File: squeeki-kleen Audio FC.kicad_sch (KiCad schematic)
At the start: 18 parts, among them J1 GND, J2 VCC, J3 P1, J4 P2, J5 C8, J6 GND out, U1 OPA1671IDCKT

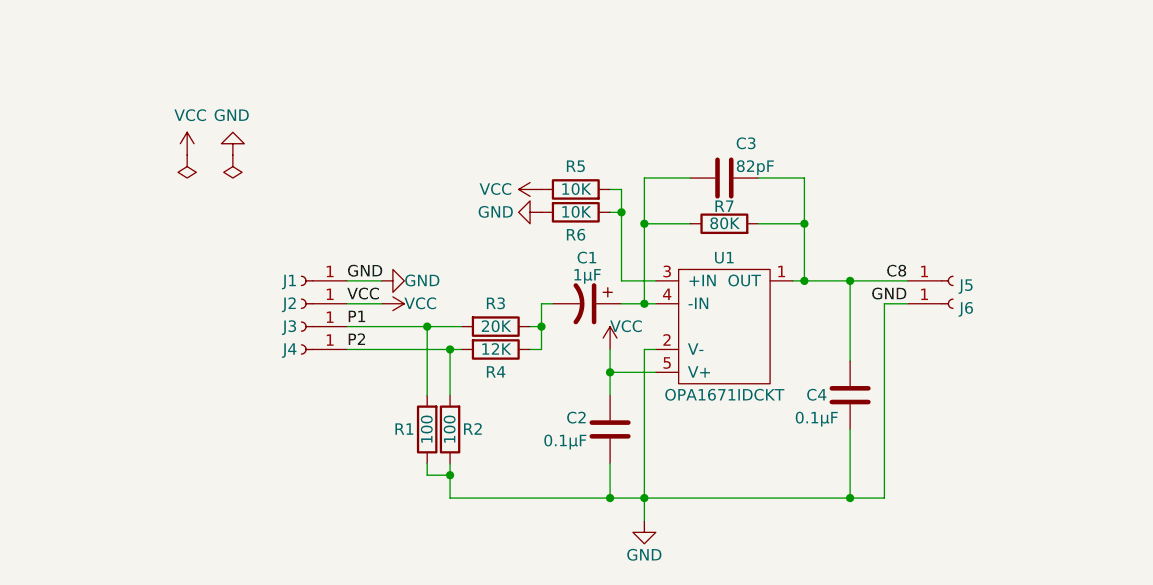
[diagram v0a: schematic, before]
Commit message: Update board layout, add level adjustment
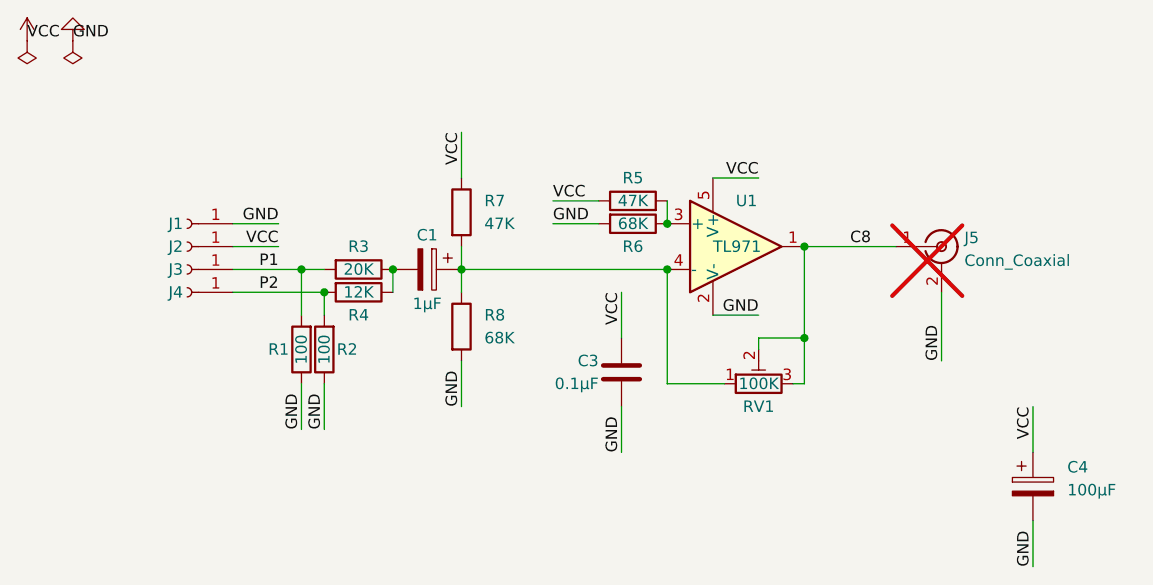
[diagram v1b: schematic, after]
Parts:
- removed C1: 1µF, Capacitor_Tantalum_SMD:CP_EIA-3216-18_Kemet-A_Pad1.58x1.35mm_HandSolder, symbol Device:CP1
- removed C3: 82pF, Capacitor_SMD:C_0805_2012Metric_Pad1.18x1.45mm_HandSolder, symbol Device:C
- removed C4: 0.1µF, Capacitor_SMD:C_0805_2012Metric_Pad1.18x1.45mm_HandSolder, symbol Device:C
- removed J5: C8, custom footprints:Custom_Pad, symbol Connector:Conn_01x01_Female
- removed J6: GND out, custom footprints:Custom_Pad, symbol Connector:Conn_01x01_Female
- removed U1: OPA1671IDCKT, Package_TO_SOT_SMD:SOT-353_SC-70-5, symbol custom_symbols:OPA1671IDCKT
- added C1: 1µF, Capacitor_SMD:CP_Elec_4x5.4, symbol Device:C_Polarized
- added C4: 100µF, Capacitor_SMD:CP_Elec_6.3x4.5, symbol Device:C_Polarized
- added J5: Conn_Coaxial, Connector_Coaxial:MMCX_Molex_73415-0961_Horizontal_0.8mm-PCB, symbol Connector:Conn_Coaxial
- added R8: 68K, Resistor_SMD:R_0805_2012Metric_Pad1.20x1.40mm_HandSolder, symbol Device:R
- added RV1: 100K, Potentiometer_SMD:Potentiometer_Bourns_3224W_Vertical, symbol Device:R_Potentiometer_Trim
- added U1: TL971, Package_TO_SOT_SMD:SOT-23-5, symbol Amplifier_Operational:MCP601-xOT
- R5: value 10K -> 47K
- R6: value 10K -> 68K
- R7: value 80K -> 47K
- renumbered C2 to C3
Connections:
- net C8: now also J5.1 (In), RV1.2, RV1.3, U1.1; no longer R7.2
- net GND: now also C4.2, J5.2 (Ext), R8.2, U1.2 (V-)
- net VCC: now also R7.1, C4.1, U1.5 (V+)
- net at R3.1, R4.1: now also C1.2
- net at R5.2, R6.1: now also U1.3 (+)
- new net: C1.1, R7.2, R8.1, RV1.1, U1.4 (-)
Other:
- moved on the sheet: C3, J1, J2, J3, J4, R1, R2, R3, R4, R5, R6
